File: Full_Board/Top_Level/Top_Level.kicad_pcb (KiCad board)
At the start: 2 copper layers, 97.8 x 174 mm, 222 parts, among them IC1 DRV8824QPWPRQ1, IC2 DRV8824QPWPRQ1, IC3 DRV8824QPWPRQ1, IC5 CD74HC4051PWT, IC6 CD74HC4051PWT, IC7 DRV8210DRLR, J1 OQ0212500000G, J1-J1 Conn_01x10, J10 KLDHCX-8-0202-A, J11 OQ0212500000G, J12 OQ0432500000G, J13 OQ0432500000G, J14 OQ0432500000G, J15 OQ0432500000G, J16 OQ0432500000G, J17 OQ0432500000G, J18 OQ0432500000G, J19 OQ0432500000G, J2 OQ0212500000G, J20 OQ0212500000G, J21 OQ0212500000G, J22 OQ0212500000G, J23 OQ0212500000G, J3 OQ0432500000G, J4 OQ0432500000G, J4-J1 Conn_01x10, J5 OQ0432500000G, J5-J1 Conn_01x10, J7 OQ0212500000G, J8 OQ0212500000G, J8-J1 Conn_01x10, J9 OQ0212500000G, U10 LM2576SX-3.3-NOPB, U11 SOD_01H.TCT_SEM, U12 SOD_01H.TCT_SEM, U13 SOD_01H.TCT_SEM, U14 SOD_01H.TCT_SEM, U16 SOD_01H.TCT_SEM, U17 SOD_01H.TCT_SEM, U18 SOD_01H.TCT_SEM, U3 SOD_01H.TCT_SEM, U4 SOD_01H.TCT_SEM, U5 SOD_01H.TCT_SEM, U6 SOD_01H.TCT_SEM, U7 JS102011SCQN, U8 SOD_01H.TCT_SEM, U9 SOD_01H.TCT_SEM

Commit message: Adjustments in prep for silkscreen
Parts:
- U11, U12, U13, U14, U16, U17, U18, U3, U4, U5, U6, U8, U9, locked (x3): value SOD_01H.TCT_SEM -> UCLAMP3301H.TCT
- moved JP5 6.35 mm to (113.8, 34.3)
- moved R23 6.35 mm to (114.8, 27.2)
- moved C15 6.35 mm to (118.9, 28.4)
- moved R24 6.35 mm to (116.6, 29.9)
- moved R25 6.35 mm to (119.4, 32.8)
- moved S2 6.35 mm to (120.6, 23.4)
- moved C14 3.05 mm to (102.1, 28.4)
- moved JP4 3.05 mm to (97.3, 34.3)
- moved R20 3.05 mm to (98.0, 27.2)
- moved R21 3.05 mm to (100.1, 29.9)
- moved R22 3.05 mm to (102.6, 32.8)
- moved S1 3.05 mm to (104.1, 23.4)
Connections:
- J4-J1 pad 2: /MSP432E401Y/PF_1 -> RESET_OUT
- J4-J1 pad 3: /MSP432E401Y/PM_3 -> HOME_OUT
- J4-J1 pad 4: /MSP432E401Y/PF_2 -> START_OUT
- J5-J1 pad 15: HOME_OUT -> /MSP432E401Y/PK_3
- J8-J1 pad 4: RESET_OUT -> /MSP432E401Y/PK_4
- J8-J1 pad 6: START_OUT -> /MSP432E401Y/PK_5
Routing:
- net Net-(IC6-Pad15): track 0.00 -> 63.6 mm
- net Net-(IC6-Pad1): track 63.6 -> 0.00 mm
- net RESET_OUT: vias 13 -> 0
- net GND: vias 37 -> 50
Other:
- board text added: "Black"
- board text added: "White"

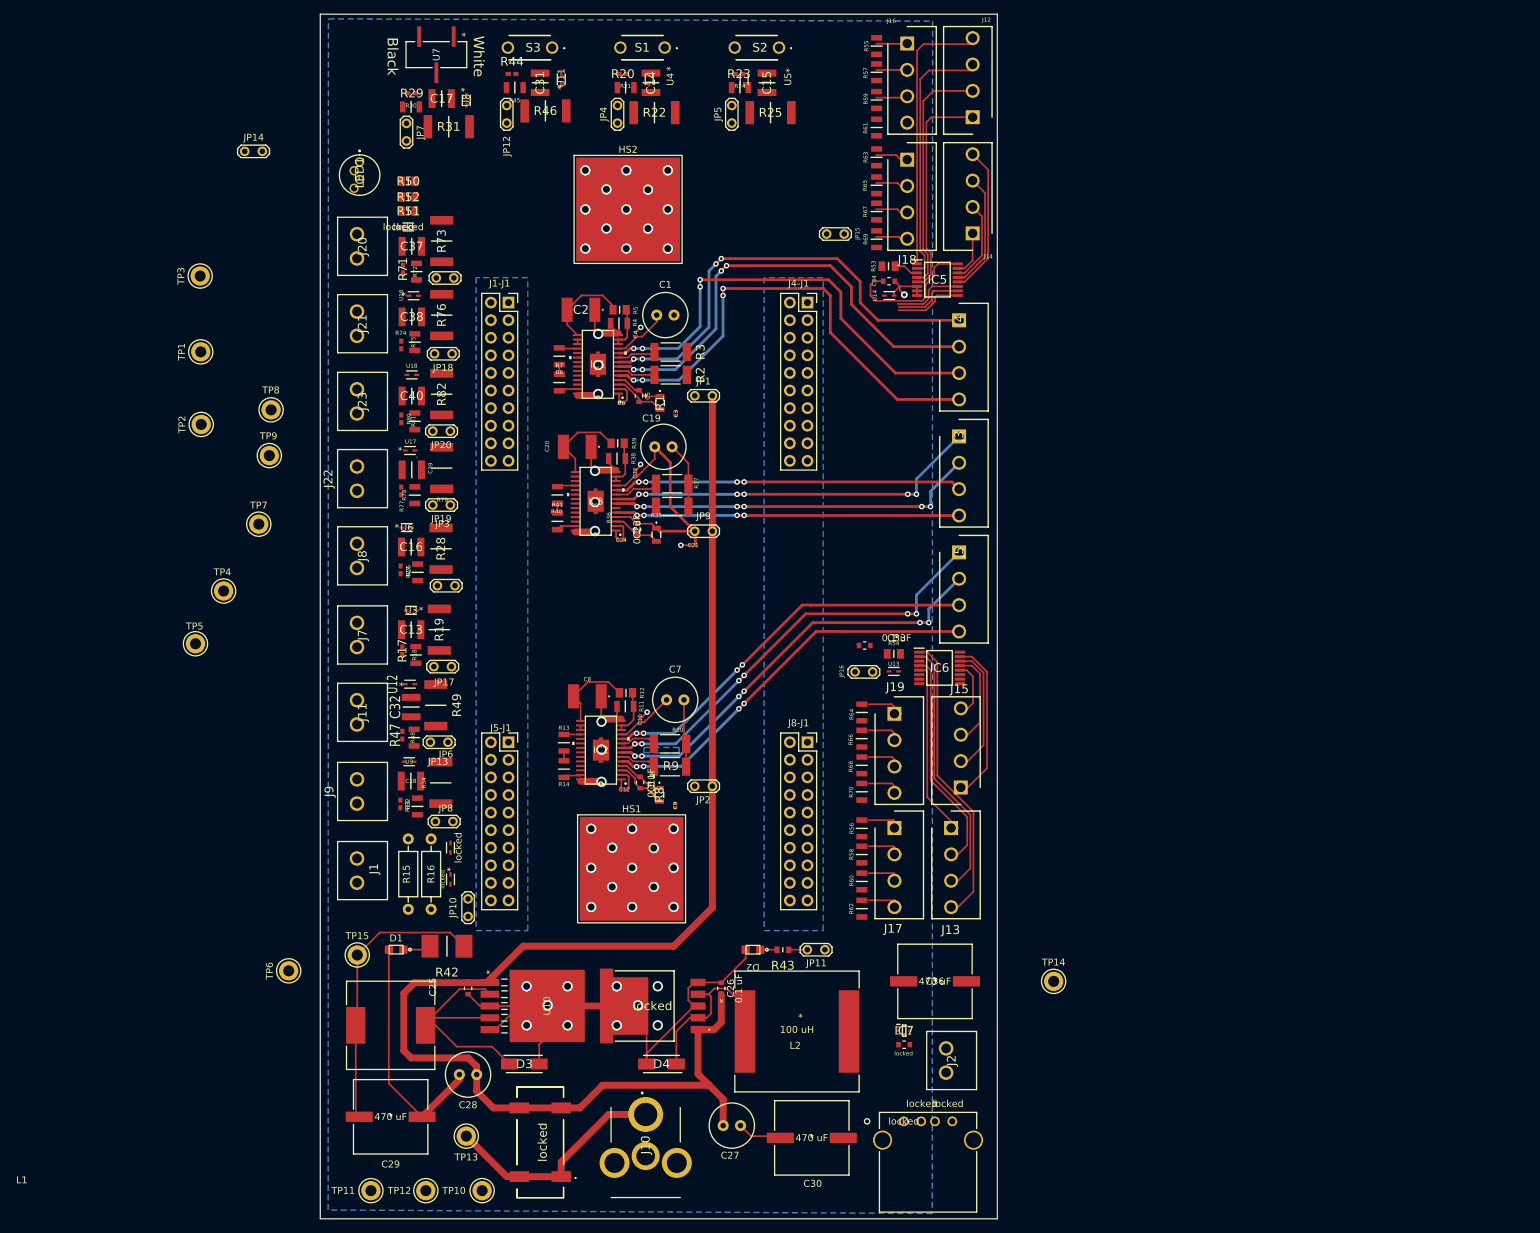
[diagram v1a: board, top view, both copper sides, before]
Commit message: Adjusted silkscreen
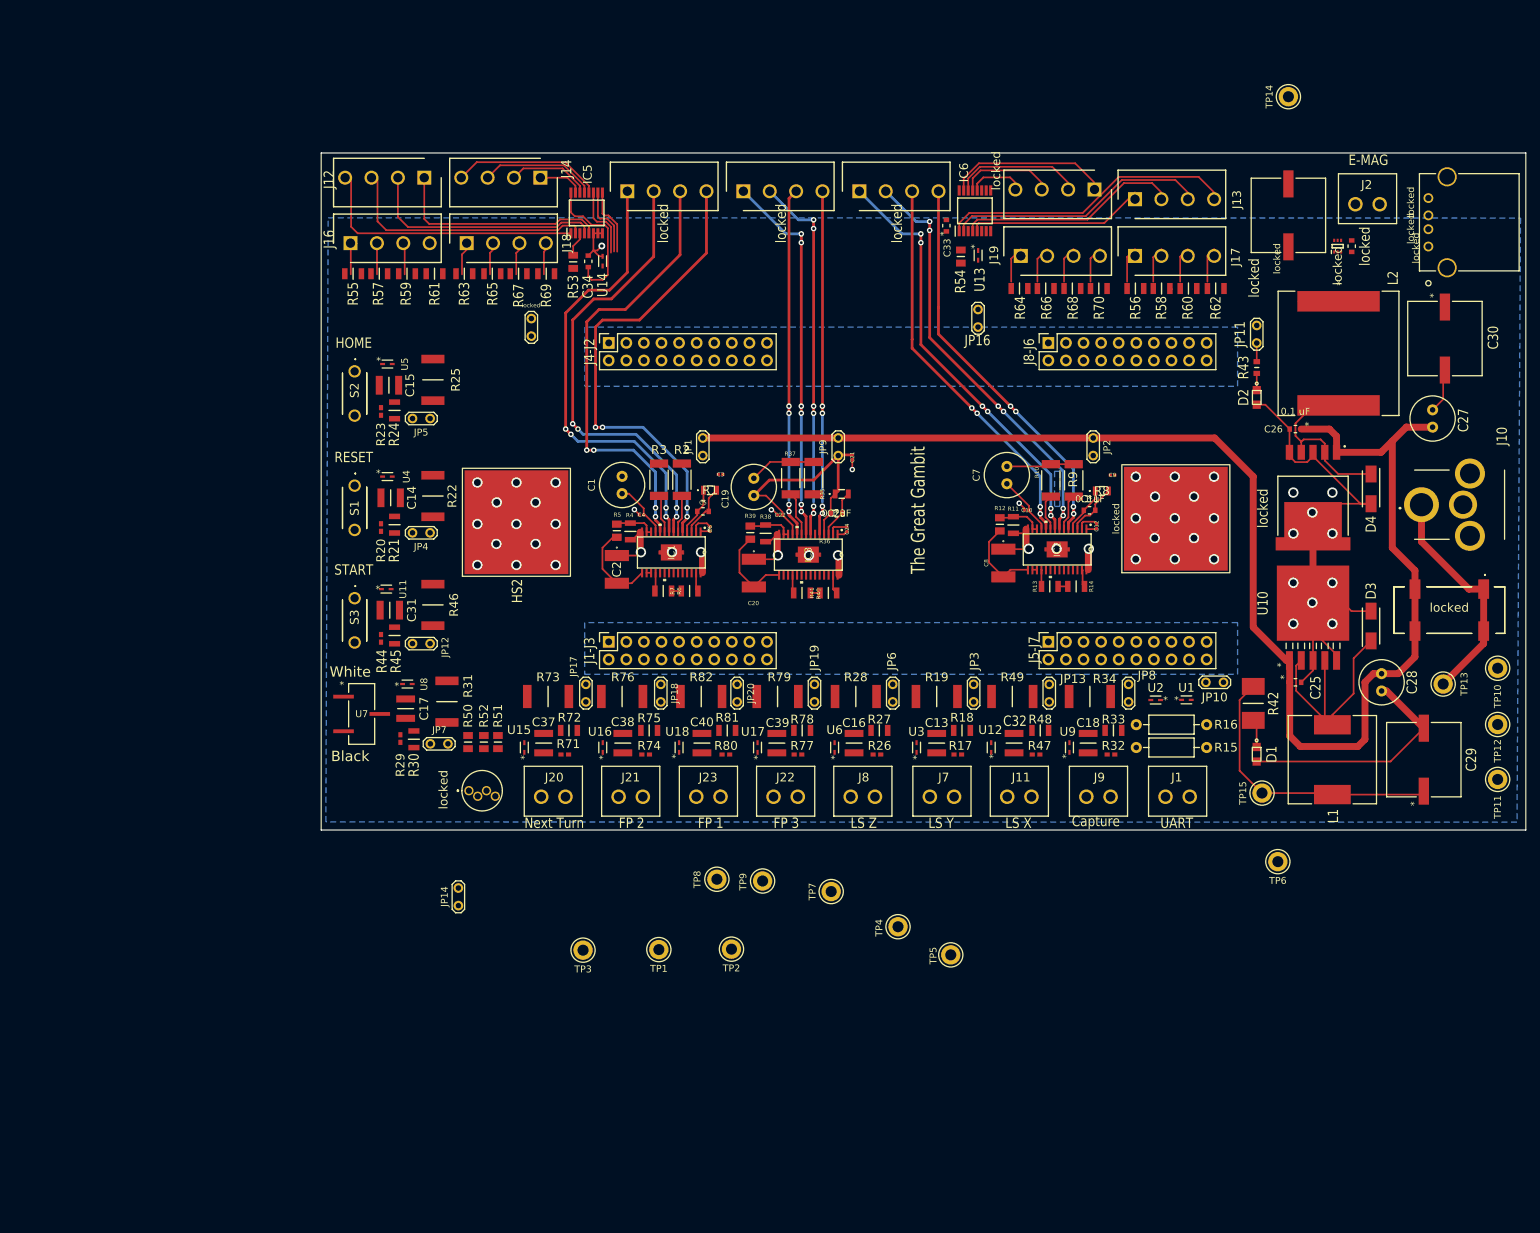
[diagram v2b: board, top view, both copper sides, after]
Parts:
- locked: renamed from C36; value 470 uF -> locked
- moved TP11 173.2 mm to (224.4, 129.1), turned to 90 degrees
- moved TP12 168.8 mm to (224.4, 121.1), turned to 90 degrees
- moved TP10 165.0 mm to (224.4, 113.0), turned to 90 degrees
- moved C29 157.9 mm to (213.7, 126.2), turned to 90 degrees
- moved TP13 155.5 mm to (216.5, 115.3), turned to 90 degrees
- moved locked 152.2 mm to (217.4, 104.6), turned to 180 degrees
- moved locked 147.3 mm to (214.4, 52.1), turned to 90 degrees
- moved C30 147.3 mm to (216.8, 65.4), turned to -90 degrees
- moved C27 143.8 mm to (215.0, 78.2), turned to 90 degrees
- moved TP6 143.7 mm to (192.7, 140.9), turned to 180 degrees
- moved C28 143.0 mm to (207.6, 113.8), turned to -90 degrees
- moved J10 142.5 mm to (213.4, 89.4), turned to 180 degrees
- moved L1 141.3 mm to (200.5, 126.2), turned to 90 degrees
- moved D3 137.7 mm to (206.1, 106.9), turned to 90 degrees
- moved J2 135.5 mm to (203.9, 46.0), turned to 0 degrees
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- renumbered J1-J1 to J1-J3, J4-J1 to J4-J2, J5-J1 to J5-J7, J8-J1 to J8-J6, locked to U1, locked to U15, locked to U2, IC7 to locked, J5 to locked, J15 to locked, JP15 to locked, LED1 to locked, J4 to locked, HS1 to locked, J3 to locked
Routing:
- net Net-(IC6-Pad15): track 63.6 -> 0.00 mm
- net Net-(IC6-Pad1): track 0.00 -> 63.6 mm
- net GND: track 185.0 -> 183.9 mm
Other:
- board size 97.8 x 174 mm -> 174 x 97.8 mm
- board text added: "Capture"
- board text added: "E-MAG"
- board text added: "FP 1"
- board text added: "FP 2"
- board text added: "FP 3"
- board text added: "HOME"
- board text added: "LS X"
- board text added: "LS Y"
- board text added: "LS Z"
- board text added: "Next Turn"
- board text added: "RESET"
- board text added: "START"
- board text added: "The Great Gambit"
- board text added: "UART"

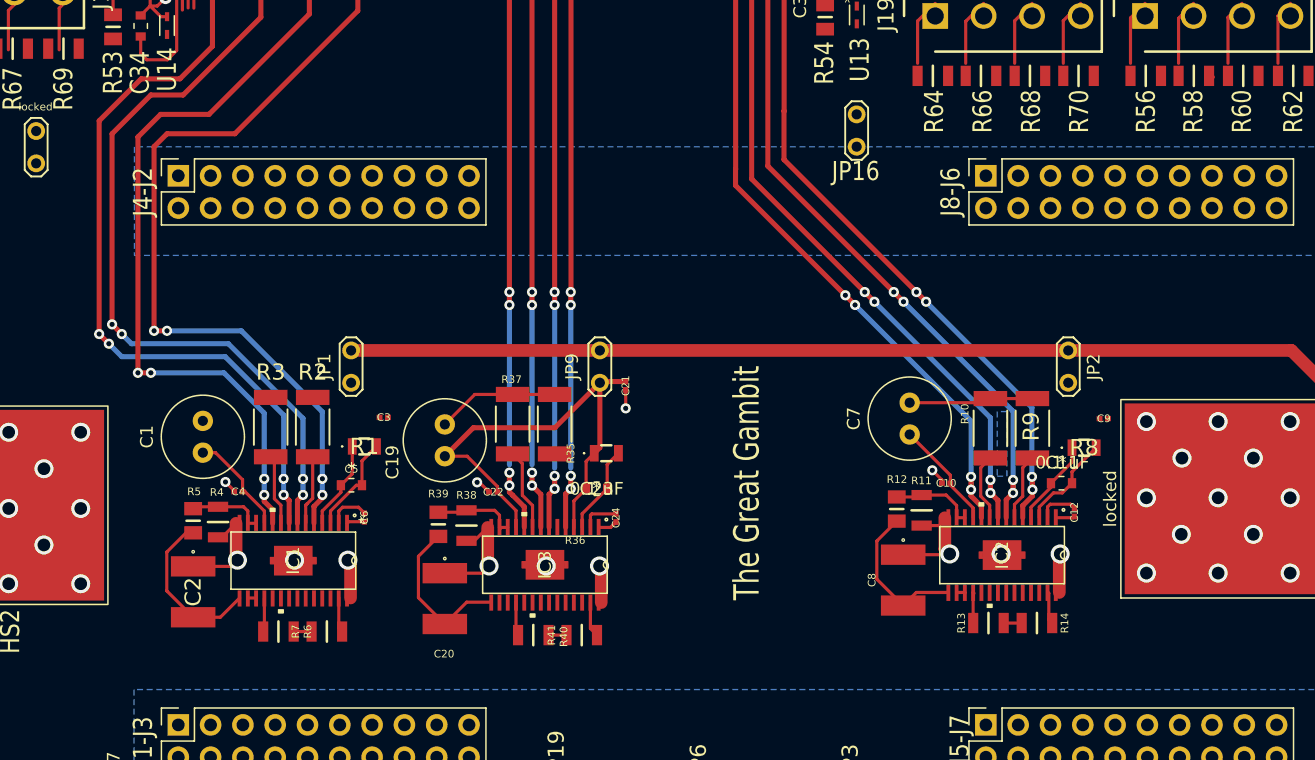
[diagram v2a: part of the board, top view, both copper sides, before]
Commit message: More silkscreen
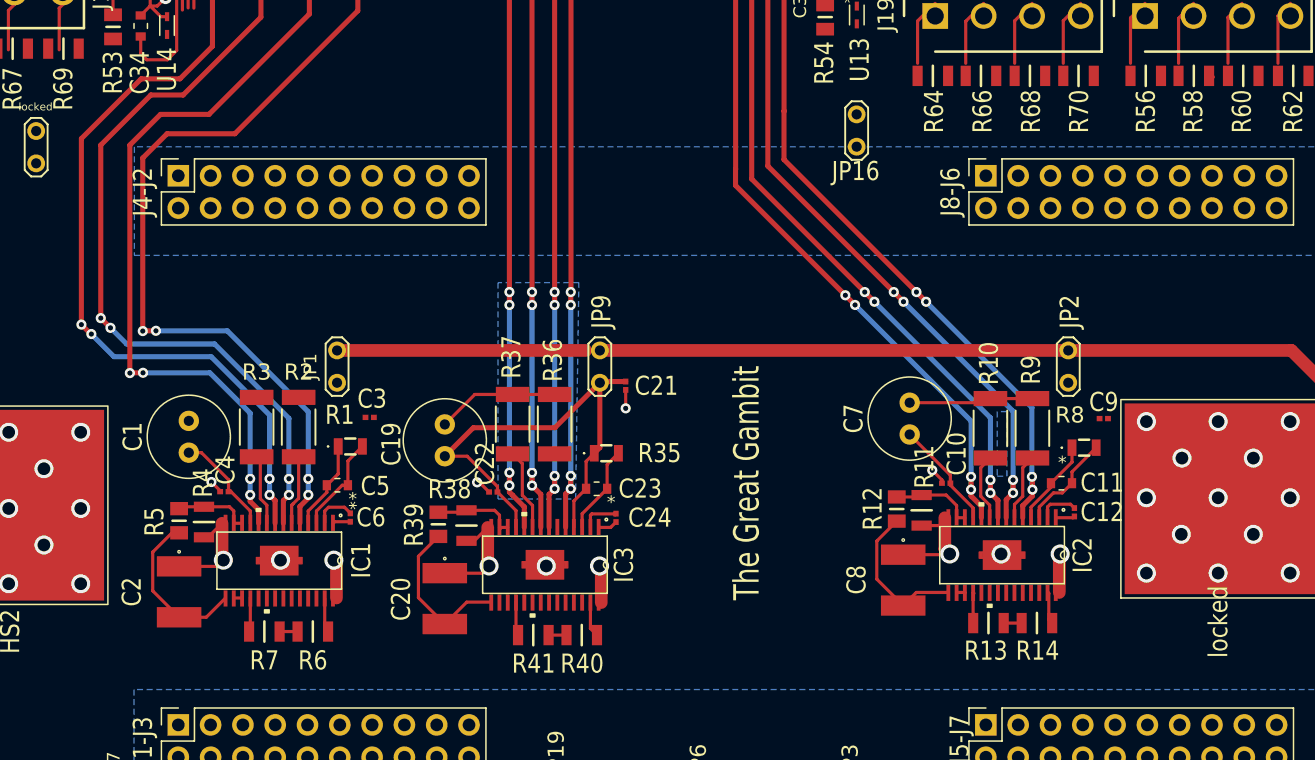
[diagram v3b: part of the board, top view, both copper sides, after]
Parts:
- moved C1 1.10 mm to (96.8, 87.8)
- moved C2 1.10 mm to (96.1, 98.7)
- moved C3 1.10 mm to (111.1, 85.0)
- moved C4 1.10 mm to (99.6, 90.9)
- moved C5 1.10 mm to (108.5, 90.4)
- moved C6 1.10 mm to (109.5, 92.9)
- moved IC1 1.10 mm to (103.9, 96.3)
- moved JP1 1.10 mm to (108.5, 79.8)
- moved R1 1.10 mm to (109.5, 87.3)
- moved R2 1.10 mm to (105.5, 85.8)
- moved R3 1.10 mm to (102.2, 85.8)
- moved R4 1.10 mm to (98.8, 91.6)
- moved R5 1.10 mm to (96.1, 93.1)
- moved R6 1.10 mm to (101.2, 101.1)
- moved R7 1.10 mm to (105.0, 101.1)
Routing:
- net /StepperDriver1/2A: track 54.3 -> 55.9 mm
- net /StepperDriver1/2B: track 55.3 -> 56.9 mm
- net /StepperDriver1/1B: track 49.9 -> 51.5 mm
- net /StepperDriver1/1A: track 49.1 -> 50.8 mm

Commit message: Some traces
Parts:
- moved R7 6.37 mm to (111.2, 102.3), turned to 180 degrees
- moved R14 5.81 mm to (167.6, 101.6), turned to 180 degrees
- moved R41 5.75 mm to (131.8, 102.3), turned to 180 degrees
- moved R13 3.64 mm to (156.0, 103.4), turned to 90 degrees
- moved R40 3.48 mm to (119.9, 103.9), turned to 90 degrees
- moved R6 1.91 mm to (102.3, 102.6), turned to 180 degrees
- moved JP16 1.02 mm to (149.4, 62.7)
- moved C9 0.13 mm to (168.7, 85.1)
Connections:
- J1-J3 pad 10: /MSP432E401Y/PC_6 -> COLOR_OUT
- J1-J3 pad 11: XYZ_DECAY -> Y_ENABLE
- J1-J3 pad 12: /MSP432E401Y/PE_5 -> NEXT_TURN_OUT
- J1-J3 pad 13: XYZ_RESET -> Y_STEP
- J1-J3 pad 14: /MSP432E401Y/PD_3 -> X_FAULT
- J1-J3 pad 15: XY_MS2 -> XY_MS0
- J1-J3 pad 16: COLOR_OUT -> X_STEP
- J1-J3 pad 18: NEXT_TURN_OUT -> X_ENABLE
- J1-J3 pad 19: XY_MS0 -> XY_MS2
- J1-J3 pad 20: /MSP432E401Y/PB_3 -> X_DIR
- J1-J3 pad 5: Y_DIR -> XYZ_RESET
- J1-J3 pad 7: Y_ENABLE -> XYZ_DECAY
- J1-J3 pad 9: Y_STEP -> Y_DIR
- J4-J2 pad 10: X_ENABLE -> /MSP432E401Y/PL_4
- J4-J2 pad 12: X_DIR -> /MSP432E401Y/PL_5
- J4-J2 pad 14: X_STEP -> /MSP432E401Y/PL_0
- J4-J2 pad 18: X_FAULT -> /MSP432E401Y/PL_2
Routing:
- net GND: track 183.9 -> 376.7 mm, vias 50 -> 54
- net XYZ_DECAY: track 0.00 -> 37.7 mm, vias 0 -> 2
- net XY_MS0: track 0.00 -> 35.2 mm, vias 0 -> 1
- net XY_MS1: track 0.00 -> 34.9 mm, vias 0 -> 1
- net XY_MS2: track 0.00 -> 34.5 mm
- net MAG_IN2: track 0.00 -> 34.0 mm
- net MAG_IN1: track 0.00 -> 32.3 mm
- net Z_STEP: track 0.00 -> 28.9 mm
- net Z_ENABLE: track 0.00 -> 27.0 mm
- net Z_DIR: track 0.00 -> 26.3 mm
- net X_STEP: track 0.00 -> 24.6 mm, vias 0 -> 1
- net Net-(IC6-Pad15): track 0.00 -> 23.0 mm
- net Net-(IC6-Pad1): track 63.6 -> 42.1 mm
- net X_ENABLE: track 0.00 -> 20.4 mm, vias 0 -> 1
- net Z_MS2: track 0.00 -> 18.5 mm, vias 0 -> 1
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
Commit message: More traces
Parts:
- added J16: OQ0432500000G, OQ0432500000G:RHDR4W80P0X381_1X4_1540X700X920P, F.Cu at (58.7, 51.6)
- moved JP14 35.0 mm to (81.5, 113.0), turned to 180 degrees
- moved locked 25.0 mm to (79.0, 105.9), turned to -90 degrees
- moved R50 20.2 mm to (84.9, 105.7), turned to 180 degrees
- moved R52 17.2 mm to (84.9, 108.0), turned to 180 degrees
- moved R51 14.5 mm to (84.9, 110.0), turned to 180 degrees
- moved HS2 4.55 mm to (82.8, 87.4)
- moved JP7 2.37 mm to (72.6, 124.0), turned to 180 degrees
- moved locked 2.05 mm to (84.9, 60.5), turned to 0 degrees
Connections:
- J1-J3 pad 4: LED_B -> LED_G
- J1-J3 pad 8: LED_G -> LED_B
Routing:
- net +3.3V: track 20.5 -> 210.2 mm
- net GND: track 376.7 -> 428.4 mm, vias 54 -> 56
- net +5V: track 10.5 -> 54.0 mm
- net Net-(C30-Pad1): track 8.47 -> 38.5 mm
- net LS_X_OUT: track 6.69 -> 34.6 mm
- net DEMUX_S2: track 9.76 -> 30.7 mm, vias 0 -> 1
- net LED_B: track 0.00 -> 20.8 mm
- net DEMUX_S1: track 10.1 -> 29.4 mm, vias 0 -> 1
- net DEMUX_S0: track 10.5 -> 28.6 mm, vias 0 -> 1
- net LED_R: track 0.00 -> 16.8 mm
- net LED_G: track 0.00 -> 14.9 mm
- net U3RX: track 11.1 -> 25.0 mm, vias 0 -> 1
- net U3TX: track 4.42 -> 17.5 mm
- net Net-(JP14-Pad2): track 0.00 -> 7.37 mm
- net CAPTURE_OUT: track 6.69 -> 14.0 mm
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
